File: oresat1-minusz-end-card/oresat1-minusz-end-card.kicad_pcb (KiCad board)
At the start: 4 copper layers, 99.8 x 94.6 mm, 86 parts, among them J1 J-SAMTEC-TFM-120-01-L-D-RA, J2 U.FL-R-SMT-1, J3 Harwin M55-7101242R, J5 Harwin M55-7101242R, Q1 DMP2240UDM, Q2 PMV45EN, Q3 PMV45EN, Q4 PMV45EN, Q5 DMP2240UDM-7, Q6 PMV45EN, Q7 DMP2240UDM-7, U11 MIC842LYC5, U12 MIC842LYC5, U2 MAX7310

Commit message: v1.3, theoretically done
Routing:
- net Net-(Q2-D): track 82.1 -> 86.2 mm
- net Net-(U11-INP): track 15.4 -> 13.0 mm
- net VPD: track 45.0 -> 46.0 mm
- net Net-(Q1A-S): track 4.58 -> 5.46 mm
- net VBUS: vias 35 -> 38

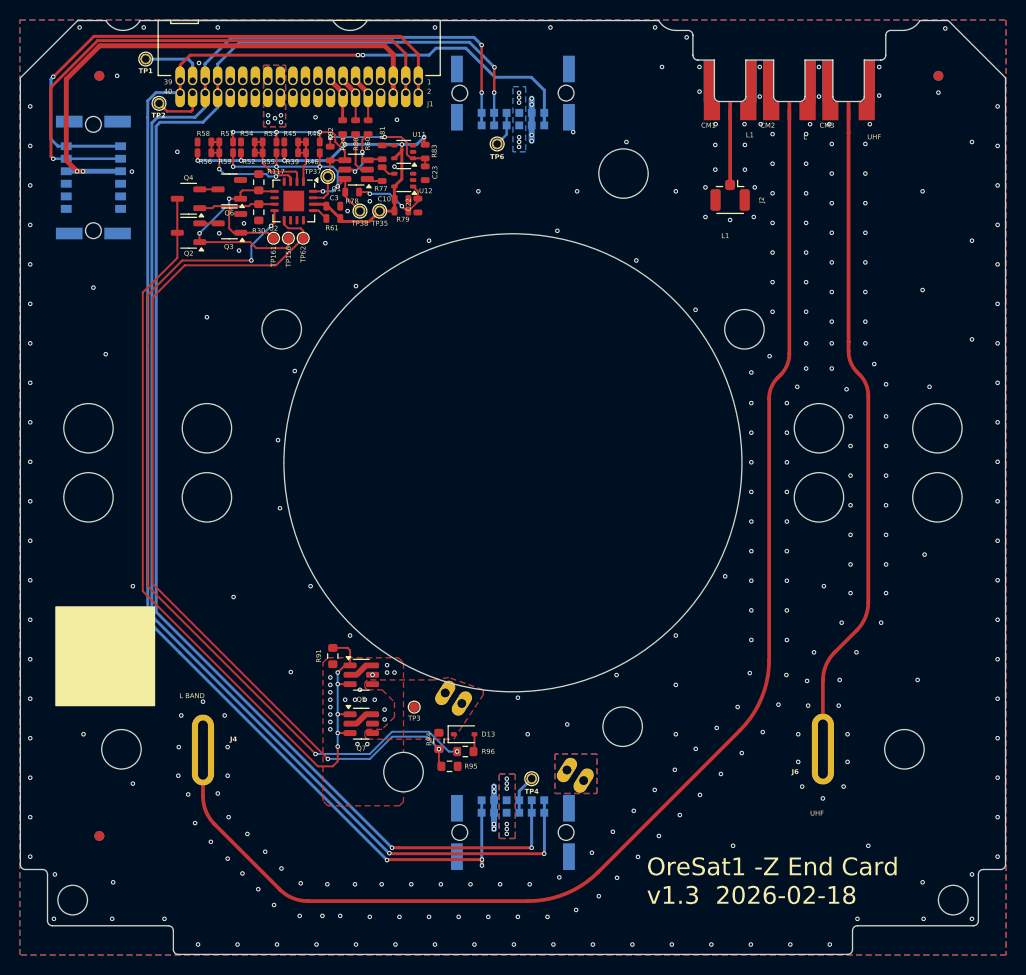
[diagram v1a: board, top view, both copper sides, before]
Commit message: OreSat1 -Z end card update
Upgraded symbols, fixed BOM and added presets, and added UART switches for new solar modules. Clleaned up layout, including some planes and footprints. Still more left to do, but it's more ready to go.
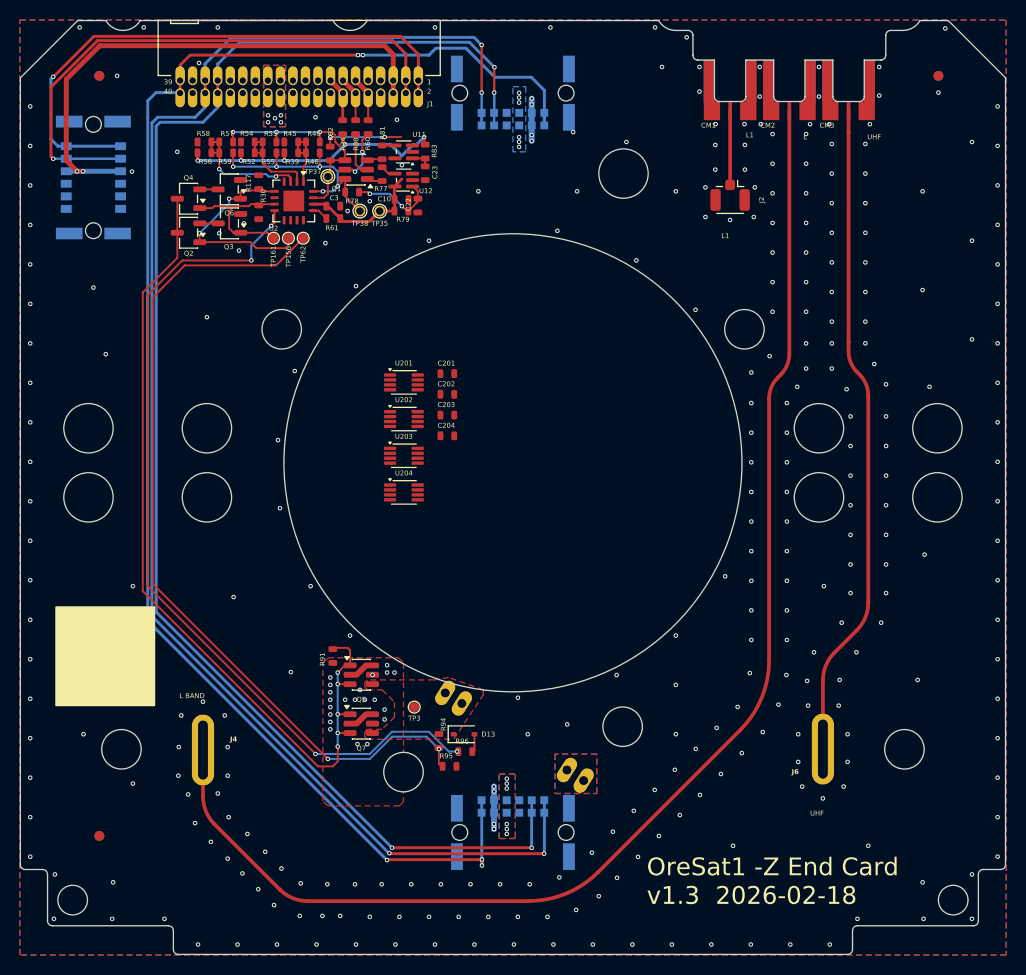
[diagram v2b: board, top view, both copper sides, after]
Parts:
- removed TP1, TP2, TP4, TP6: TEST-POINT-LARGE-SQUARE, oresat-misc:TestPoint-0.75mm-th
- added C201: 100n, oresat-passives:0603-C-NOSILK, F.Cu at (141.9, 93.5)
- added C202: 100n, oresat-passives:0603-C-NOSILK, F.Cu at (141.9, 95.6)
- added C203: 100n, oresat-passives:0603-C-NOSILK, F.Cu at (141.9, 97.7)
- added C204: 100n, oresat-passives:0603-C-NOSILK, F.Cu at (141.9, 99.8)
- added U201: TS5A21366, Package_SO:VSSOP-8_2.3x2mm_P0.5mm, F.Cu at (137.4, 94.4)
- added U202: TS5A21366, Package_SO:VSSOP-8_2.3x2mm_P0.5mm, F.Cu at (137.4, 98.1)
- added U203: TS5A21366, Package_SO:VSSOP-8_2.3x2mm_P0.5mm, F.Cu at (137.4, 101.8)
- added U204: TS5A21366, Package_SO:VSSOP-8_2.3x2mm_P0.5mm, F.Cu at (137.4, 105.5)
- CF1: value J-HARWIN-M55-6001242R -> M55-6001242R
- CM1, CM2, CM3: value J-MOLEX-SMPM-73300-003X -> 2477330-1
- J3, J5: value Harwin M55-7101242R -> M55-7101242R
- R117, R30, R91, R94, R95, R96: footprint Resistor_SMD:R_0603_1608Metric -> oresat-passives:0603-C-NOSILK
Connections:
- net OPD_PWR renamed /OPD_PWR
- net OPD_SCL renamed /OPD_SCL
- net OPD_SDA renamed /OPD_SDA
- J3 pad 7: /-X_AUX -> /MX_UART_TX
- J3 pad 8: /-X_AUX -> /MX_UART_RX
- J5 pad 7: /+X_AUX -> /PX_UART_TX
- J5 pad 8: /+X_AUX -> /PX_UART_RX
- U2 pad 10: unconnected-(U2-IO5-Pad10) -> /OPD/PY_UART_EN
- U2 pad 11: unconnected-(U2-IO6-Pad11) -> /OPD/MX_UART_EN
- U2 pad 12: unconnected-(U2-IO7-Pad12) -> /OPD/MY_UART_EN
- U2 pad 4: unconnected-(U2-IO0-Pad4) -> /OPD/READ_ANTENNAS
- U2 pad 9: /OPD/READ_ANTENNAS -> /OPD/PX_UART_EN
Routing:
- net /C3-UART-TX: track 6.65 -> 0.00 mm
- net /C3-UART-RX: track 5.51 -> 0.00 mm
- net /-X_AUX: track 3.97 -> 0.00 mm
- net VPD: track 46.0 -> 42.2 mm
- net /+X_AUX: track 3.55 -> 0.00 mm
- net /OPD/READ_ANTENNAS: track 89.8 -> 86.4 mm
- net Net-(U11-INP): track 13.0 -> 10.4 mm
- net GND: vias 311 -> 310
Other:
- board text removed: "OreSat0.5 -Z End Card ${REVISION} ${ISSUE_DATE}"
